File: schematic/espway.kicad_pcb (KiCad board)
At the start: 2 copper layers, 37.1 x 41.5 mm, 34 parts, among them J1 CONN_01X02, J2 CONN_01X02, J3 CONN_01X04_MALE, SW1 SW_Push, U1 DRV8835, U2 LM1117-3.3, U3 ESP-12E, U4 LSM6DS3

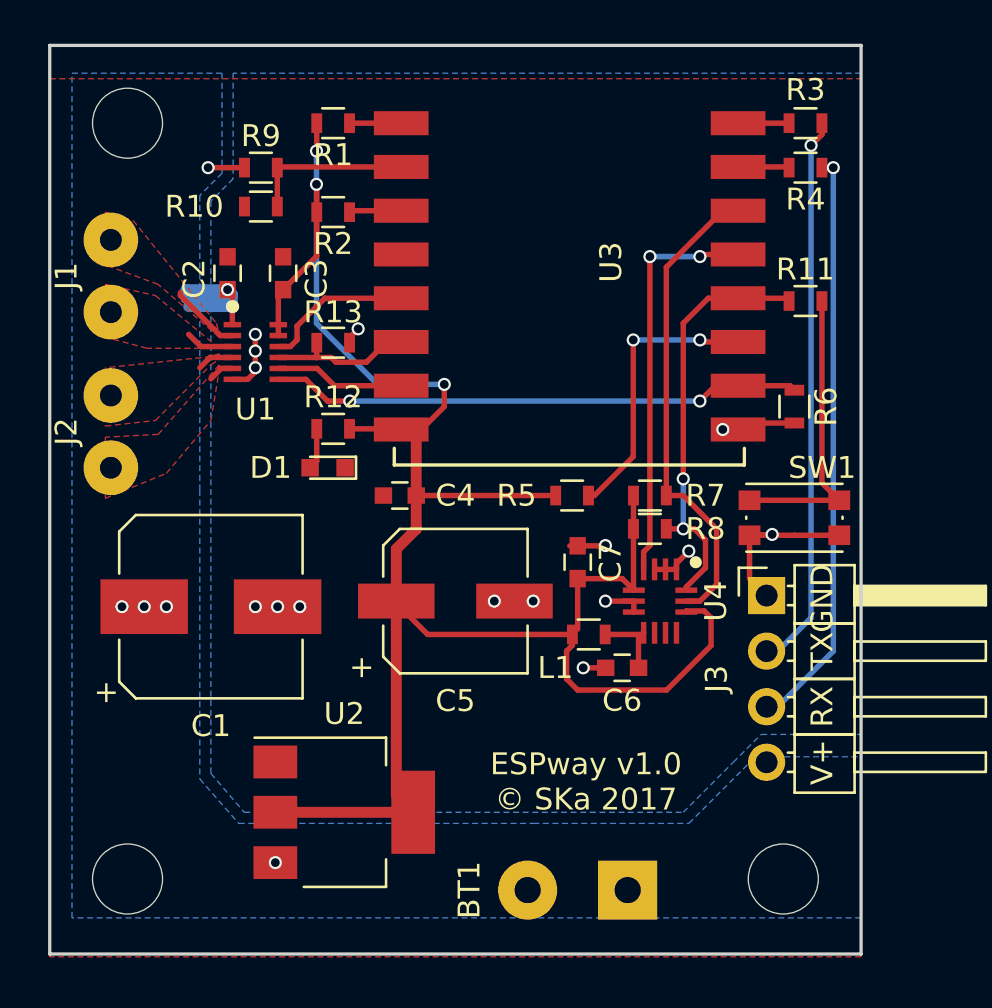
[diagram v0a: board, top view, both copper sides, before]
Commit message: PCB: improvements
Routing simplified
Use LGA-14 and WSON-12 packages supplied with KiCAD
diff --git a/schematic-old/espway-rescue.lib b/schematic-old/espway-rescue.lib
new file mode 100644
index 0000000..4d5fc14
--- /dev/null
+++ b/schematic-old/espway-rescue.lib
@@ -0,0 +1,25 @@
+EESchema-LIBRARY Version 2.3
+#encoding utf-8
+#
+# LM1117-5.0-RESCUE-espway
+#
+DEF LM1117-5.0-RESCUE-espway U 0 30 Y Y 1 F N
+F0 "U" 100 -250 50 H V C CNN
+F1 "LM1117-5.0-RESCUE-espway" 0 250 50 H V C CNN
+F2 "" 0 0 50 H V C CNN
+F3 "" 0 0 50 H V C CNN
+$FPLIST
+ SOT-223*
+ TO-263*
+ TO-252*
+$ENDFPLIST
+DRAW
+S -200 -200 200 200 0 1 10 f
+X GND/ADJ 1 0 -300 100 U 50 50 1 1 W
+X VO 2 300 0 100 L 50 50 1 1 w
+X VI 3 -300 0 100 R 50 50 1 1 W
+X VO 4 300 0 100 L 50 50 1 1 w N
+ENDDRAW
+ENDDEF
+#
+#End Library
diff --git a/schematic-old/espway.pro b/schematic-old/espway.pro
index d39d63e..2c69b71 100644
--- a/schematic-old/espway.pro
+++ b/schematic-old/espway.pro
@@ -1,4 +1,4 @@
-update=su  5. helmikuuta 2017 09.41.29
+update=2017 October 17, Tuesday 01:25:24
 version=1
 last_client=kicad
 [pcbnew]
@@ -25,43 +25,6 @@ version=1
 NetIExt=net
 [general]
 version=1
-[eeschema]
-version=1
-LibDir=
-[eeschema/libraries]
-LibName1=power
-LibName2=device
-LibName3=transistors
-LibName4=conn
-LibName5=linear
-LibName6=regul
-LibName7=74xx
-LibName8=cmos4000
-LibName9=adc-dac
-LibName10=memory
-LibName11=xilinx
-LibName12=microcontrollers
-LibName13=dsp
-LibName14=microchip
-LibName15=analog_switches
-LibName16=motorola
-LibName17=texas
-LibName18=intel
-LibName19=audio
-LibName20=interface
-LibName21=digital-audio
-LibName22=philips
-LibName23=display
-LibName24=cypress
-LibName25=siliconi
-LibName26=opto
-LibName27=atmel
-LibName28=contrib
-LibName29=valves
-LibName30=d1_mini
-LibName31=gy-521
-LibName32=ws2812b
-LibName33=l293d
 [schematic_editor]
 version=1
 PageLayoutDescrFile=
@@ -72,3 +35,41 @@ NetFmtName=
 SpiceForceRefPrefix=0
 SpiceUseNetNumbers=0
 LabSize=60
+[eeschema]
+version=1
+LibDir=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
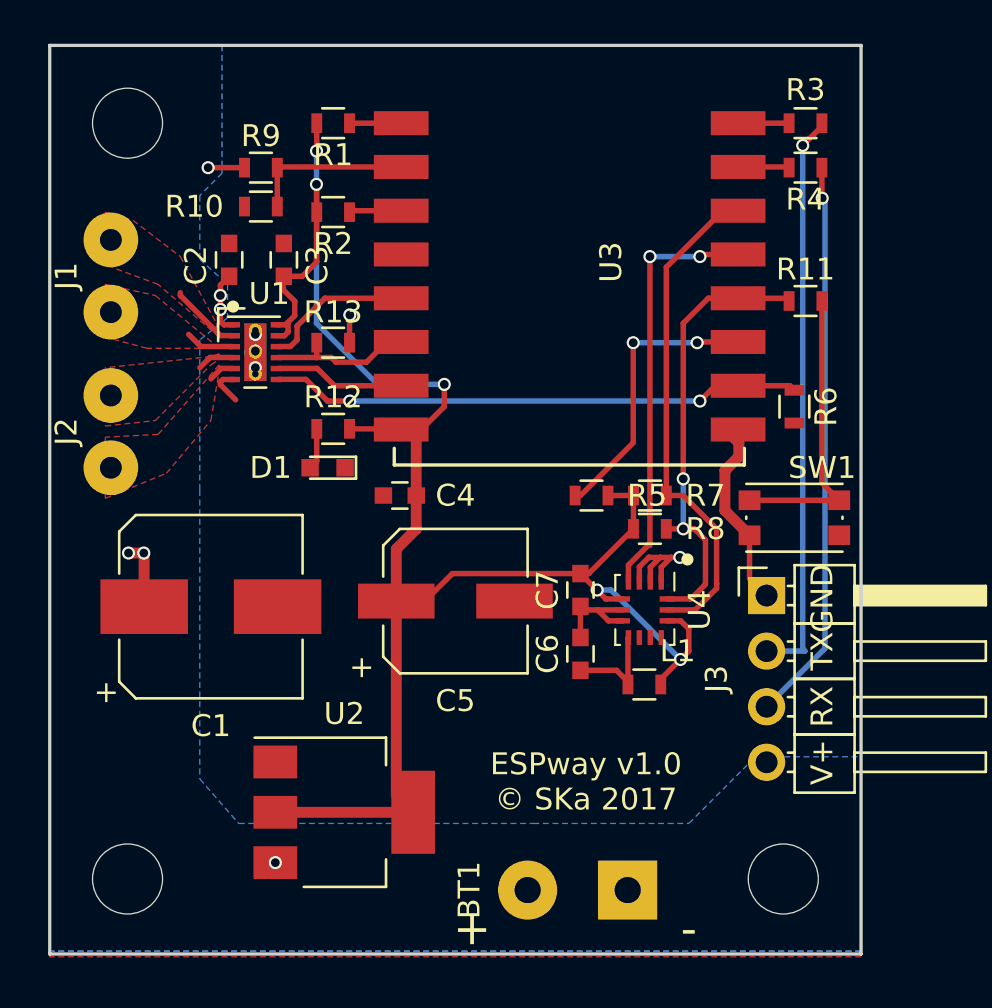
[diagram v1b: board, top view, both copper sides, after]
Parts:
- U1: footprint espway-modules:WSON-12 -> Housings_SON:WSON-12-1EP_3x2mm_Pitch0.5mm_ThermalVias
- U4: footprint espway-modules:LGA-14L -> Housings_LGA:Bosch_LGA-14_3x2.5mm_Pitch0.5mm
- moved L1 3.42 mm to (170.4, 108.0), turned to 0 degrees
- moved U1 2.74 mm to (152.7, 92.8)
- moved U4 2.09 mm to (170.5, 104.5)
- moved C6 2.01 mm to (167.5, 106.6), turned to 90 degrees
- moved C7 1.28 mm to (167.5, 103.6), turned to 90 degrees
- moved R5 0.89 mm to (168.0, 99.3), turned to 180 degrees
- moved C2 0.62 mm to (151.5, 88.5)
- moved C3 0.61 mm to (154.0, 88.5)
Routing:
- net +3V3: track 92.1 -> 83.7 mm, vias 3 -> 5
- net +BATT: track 12.7 -> 7.97 mm, vias 7 -> 6
- net GND: track 27.7 -> 24.7 mm, vias 15 -> 5
- net SDA: track 19.4 -> 20.8 mm
- net Net-(J3-Pad2): track 25.7 -> 27.1 mm
- net Net-(C6-Pad1): track 3.48 -> 4.72 mm
- net SCL: track 21.3 -> 22.5 mm
- net INT: track 17.8 -> 18.8 mm
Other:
- board text added: "+"
- board text added: "-"

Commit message: PCB update before rerouting
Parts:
- moved R6 25.5 mm to (151.9, 96.9)
- moved R11 21.4 mm to (173.2, 111.4), turned to 270 degrees
- moved SW1 13.7 mm to (169.1, 111.3)
- moved R5 9.80 mm to (172.6, 108.0), turned to 0 degrees
- moved C4 3.52 mm to (156.7, 96.9), turned to 270 degrees
- moved D1 2.73 mm to (153.5, 96.9), turned to 90 degrees
- moved R4 1.52 mm to (177.3, 85.7), turned to 90 degrees
- moved C2 1.46 mm to (152.8, 89.2)
- moved R12 1.34 mm to (155.1, 96.9), turned to 90 degrees
- moved BT1 1.02 mm to (165.1, 116.3)
- moved R3 1.01 mm to (177.3, 83.1), turned to 90 degrees
- moved J2 0.90 mm to (146.9, 104.8)
- moved J1 0.89 mm to (146.9, 90.9)
- moved C3 0.78 mm to (154.4, 89.2)
- moved L1 0.66 mm to (169.8, 108.0)
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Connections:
- R3 pad 1: Net-(J3-Pad2) -> Net-(J3-Pad3)
- R4 pad 1: Net-(J3-Pad3) -> Net-(J3-Pad2)
- U3 pad 11: Net-(R5-Pad2) -> SCL
- U3 pad 14: SCL -> Net-(U3-Pad14)
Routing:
- net GND: track 24.7 -> 43.8 mm, vias 5 -> 18
- net Net-(U3-Pad14): track 0.00 -> 16.7 mm
- net SCL: track 22.5 -> 37.4 mm
- net INT: track 18.8 -> 6.15 mm, vias 2 -> 0
- net Net-(R5-Pad2): track 12.5 -> 2.16 mm, vias 2 -> 0
- net Net-(R11-Pad2): track 13.7 -> 6.95 mm
- net Net-(J3-Pad2): track 27.1 -> 20.6 mm, vias 1 -> 0
- net ADC: track 8.15 -> 13.1 mm
- net Net-(J2-Pad1): track 1.18 -> 4.55 mm
- net Net-(R2-Pad1): track 3.09 -> 0.09 mm
- net +BATT: track 7.97 -> 5.53 mm, vias 6 -> 0
- net Net-(J1-Pad1): track 2.23 -> 4.17 mm
- net Net-(J2-Pad2): track 1.68 -> 3.58 mm
- net Net-(J1-Pad2): track 3.27 -> 4.21 mm
- net GPIO15: track 24.5 -> 25.2 mm
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- added copper zone on F.Cu, net +BATT
- removed copper zone on B.Cu, net +BATT
- removed copper zone on F.Cu, net GND
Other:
- board size 37.1 x 41.5 mm -> 37.1 x 41.7 mm
- board text removed: "ESPway v1.0 © SKa 2017"

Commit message: Initial work on new PCB
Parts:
- removed ?: MountingHole_2.2mm_M2, Mounting_Holes:MountingHole_3.2mm_M3
- removed the REF** at (176.8, 116.8)
- removed the REF** at (146.8, 82.3)
- added R14: 2k2, Resistors_SMD:R_0603, F.Cu at (135.2, 134.5)
- added REF**: MountingHole_3.2mm_M3, Mounting_Holes:MountingHole_3.2mm_M3, F.Cu at (129.5, 154.0)
- added REF**: MountingHole_3.2mm_M3, Mounting_Holes:MountingHole_3.2mm_M3, F.Cu at (162.5, 123.8)
- added REF**: MountingHole_3.2mm_M3, Mounting_Holes:MountingHole_3.2mm_M3, F.Cu at (129.5, 124.0)
- C1: value 470u -> 100n; footprint Capacitors_SMD:CP_Elec_8x10 -> Capacitors_SMD:C_0603
- C2: value 100n -> 470u; footprint Capacitors_SMD:C_0603 -> Capacitors_SMD:CP_Elec_8x10
- C4: value 100n -> 100u; footprint Capacitors_SMD:C_0603 -> Capacitors_SMD:CP_Elec_6.3x5.8
- C5: value 100u -> 100n; footprint Capacitors_SMD:CP_Elec_6.3x5.8 -> Capacitors_SMD:C_0603
- R10, R5, R6: value 10k -> 470
- R11: value 470 -> 82k
- R12, R4: value 470 -> 10k
- R13: value 10k -> 2k2
- R7, R8: value 2k2 -> 10k
- R9: value 82k -> 10k
- U1: value DRV8835 -> LM1117-3.3; footprint Housings_SON:WSON-12-1EP_3x2mm_Pitch0.5mm_ThermalVias -> TO_SOT_Packages_SMD:SOT-223
- U2: value LM1117-3.3 -> ESP-12E; footprint TO_SOT_Packages_SMD:SOT-223 -> ESP8266:ESP-12E_SMD
- U3: value ESP-12E -> DRV8835; footprint ESP8266:ESP-12E_SMD -> espway-modules:WSON-12
- U4: footprint Housings_LGA:Bosch_LGA-14_3x2.5mm_Pitch0.5mm -> espway-modules:LGA-14L
- moved R3 69.3 mm to (135.5, 138.5), turned to 270 degrees
- moved R1 56.5 mm to (129.2, 132.0), turned to 270 degrees
- moved R10 55.7 mm to (149.8, 141.8), turned to 90 degrees
- moved C4 54.6 mm to (132.2, 145.8)
- moved U1 54.5 mm to (139.8, 145.8), turned to 90 degrees
- moved C2 54.0 mm to (162.5, 142.2), turned to 180 degrees
- moved U4 50.7 mm to (129.5, 134.5)
- moved L1 50.7 mm to (130.0, 139.5), turned to 180 degrees
- moved C7 49.3 mm to (129.2, 134.8)
- moved C6 48.8 mm to (130.0, 137.8), turned to 180 degrees
- moved R9 48.0 mm to (158.5, 132.0)
- moved J3 47.7 mm to (154.5, 146.5), turned to 270 degrees
- moved C3 47.6 mm to (164.0, 135.8), turned to 90 degrees
- moved U3 47.3 mm to (163.0, 129.5), turned to 180 degrees
- moved R2 47.2 mm to (133.5, 127.8), turned to 270 degrees
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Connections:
- C1 pad 1: +BATT -> +3V3
- C2 pad 1: GND -> +BATT
- C2 pad 2: +BATT -> GND
- C3 pad 2: +3V3 -> +BATT
- C5 pad 1: +3V3 -> GND
- C5 pad 2: GND -> +3V3
- R10 pad 1: ADC -> Net-(R10-Pad1)
- R11 pad 1: SDA -> +BATT
- R11 pad 2: Net-(R11-Pad2) -> ADC
- R12 pad 1: Net-(D1-Pad2) -> ADC
- R12 pad 2: +3V3 -> GND
- R13 pad 1: Net-(R13-Pad1) -> +3V3
- R13 pad 2: GND -> SCL
- R3 pad 1: Net-(J3-Pad3) -> Net-(D1-Pad2)
- R3 pad 2: Net-(R3-Pad2) -> +3V3
- R4 pad 1: Net-(J3-Pad2) -> BENBL
- R4 pad 2: Net-(R4-Pad2) -> GND
- R5 pad 1: +3V3 -> Net-(J3-Pad3)
- R6 pad 1: GPIO15 -> Net-(J3-Pad2)
- R6 pad 2: GND -> Net-(R6-Pad2)
- R7 pad 1: +3V3 -> AENBL
- R7 pad 2: SCL -> GND
- R8 pad 1: +3V3 -> APHASE
- R8 pad 2: SDA -> GND
- R9 pad 1: +BATT -> +3V3
- R9 pad 2: ADC -> BPHASE
- SW1 pad 1: GND -> Net-(R10-Pad1)
- SW1 pad 2: Net-(R11-Pad2) -> BPHASE
- U1 pad 1: +BATT -> GND
- U1 pad 2: Net-(J1-Pad2) -> +3V3
- U1 pad 3: Net-(J1-Pad1) -> +BATT
- U1 pad 4: Net-(J2-Pad2) -> +3V3
- U2 pad 1: GND -> Net-(R1-Pad1)
- U2 pad 2: +3V3 -> ADC
- U2 pad 3: +BATT -> Net-(R2-Pad1)
- U2 pad 4: +3V3 -> Net-(U2-Pad4)
- U3 pad 1: Net-(R1-Pad1) -> +BATT
- U3 pad 10: GPIO15 -> APHASE
- U3 pad 11: SCL -> +3V3
- U3 pad 12: SDA -> +3V3
- U3 pad 13: INT -> GND
- U3 pad 2: ADC -> Net-(J1-Pad2)
- U3 pad 3: Net-(R2-Pad1) -> Net-(J1-Pad1)
- U3 pad 4: Net-(U3-Pad4) -> Net-(J2-Pad2)
- U3 pad 5: Net-(U1-Pad10) -> Net-(J2-Pad1)
- U3 pad 6: Net-(R13-Pad1) -> GND
- U3 pad 7: Net-(U1-Pad8) -> BENBL
- U3 pad 8: +3V3 -> BPHASE
- U3 pad 9: GND -> AENBL
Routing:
- net +BATT: track 5.53 -> 57.6 mm
- net GND: track 43.8 -> 7.07 mm, vias 18 -> 0
- net SCL: track 37.4 -> 7.84 mm
- net GPIO15: track 25.2 -> 0.00 mm, vias 2 -> 0
- net +3V3: track 83.9 -> 60.6 mm
- net Net-(J3-Pad3): track 26.5 -> 5.31 mm
- net BPHASE: track 0.00 -> 19.2 mm
- net Net-(U3-Pad14): track 16.7 -> 0.00 mm
- net Net-(J3-Pad2): track 20.6 -> 5.64 mm
- net SDA: track 21.2 -> 7.45 mm
- net Net-(R1-Pad1): track 3.06 -> 15.5 mm
- net (no net): track 0.00 -> 11.5 mm
- net APHASE: track 0.00 -> 10.2 mm
- net AENBL: track 0.00 -> 10.1 mm
- net Net-(R13-Pad1): track 9.15 -> 0.00 mm
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- removed copper zone on F.Cu, net +BATT
- removed copper zone on B.Cu, net GND
- removed copper zone on F.Cu, net Net-(J1-Pad1)
- removed copper zone on F.Cu, net Net-(J1-Pad2)
- removed copper zone on F.Cu, net Net-(J2-Pad1)
- removed copper zone on F.Cu, net Net-(J2-Pad2)
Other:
- board outline removed
- net class Default: clearance 0.16 -> 0.2
- rule pad_to_mask_clearance: 0.2 -> 0
- rule trace_clearance: 0.16 -> 0.2
- board text removed: "+"
- board text removed: "-"
- board text removed: "GND"
- board text removed: "RX"
- board text removed: "TX"
- board text removed: "V+"

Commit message: Committing before rerouting
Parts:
- added REF**: MountingHole_3.2mm_M3, Mounting_Holes:MountingHole_3.2mm_M3, F.Cu at (162.0, 154.0)
- moved BT1 4.15 mm to (167.8, 148.6), turned to 270 degrees
- moved R2 3.50 mm to (137.0, 127.7)
- moved R11 3.40 mm to (133.6, 127.8)
- moved R9 1.00 mm to (158.5, 131.0)
- moved REF** 0.56 mm to (162.0, 124.0)
- moved J1 0.32 mm to (167.8, 126.5)
- moved R10 0.25 mm to (150.0, 141.8)
- moved R5 0.25 mm to (146.0, 141.8)
- moved R6 0.25 mm to (147.8, 141.8)
- moved J2 0.20 mm to (167.8, 120.0)
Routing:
- net +3V3: track 60.6 -> 94.6 mm
- net Net-(R5-Pad2): track 0.00 -> 21.7 mm
- net Net-(R6-Pad2): track 0.00 -> 18.9 mm
- net GND: track 7.07 -> 21.4 mm, vias 0 -> 10
- net +BATT: track 57.6 -> 69.7 mm
- net (no net): track 11.5 -> 0.00 mm
- net BPHASE: track 19.2 -> 28.3 mm
- net Net-(R2-Pad1): track 7.90 -> 3.21 mm
- net ADC: track 6.06 -> 9.16 mm
- net Net-(J1-Pad2): track 2.01 -> 0.00 mm
- net Net-(J2-Pad2): track 1.91 -> 0.00 mm
- net Net-(J1-Pad1): track 1.91 -> 0.00 mm
- net Net-(J2-Pad1): track 1.41 -> 0.00 mm
- added copper zone on B.Cu, net GND
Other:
- board outline added: 44.5 x 37 mm

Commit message: An intermediate commit
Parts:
- moved J3 25.7 mm to (130.2, 138.0), turned to 180 degrees
- moved L1 24.8 mm to (153.0, 148.8), turned to 270 degrees
- moved C7 24.3 mm to (148.5, 149.5), turned to 180 degrees
- moved C6 24.2 mm to (151.5, 148.8), turned to 270 degrees
- moved U4 23.8 mm to (148.3, 149.1), turned to 0 degrees
- moved R6 15.3 mm to (133.8, 135.5), turned to 0 degrees
- moved R5 14.5 mm to (133.8, 134.0), turned to 0 degrees
- moved R14 13.8 mm to (147.0, 141.8)
- moved R13 13.6 mm to (148.5, 141.8)
- moved R1 4.51 mm to (133.5, 130.5)
- moved C4 2.21 mm to (134.2, 144.8)
- moved U1 1.79 mm to (141.3, 144.8)
- moved R2 0.10 mm to (137.0, 127.8)
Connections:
- U2 pad 5: INT -> SCL
- U2 pad 7: SCL -> INT
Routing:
- net +3V3: track 94.6 -> 0.00 mm
- net +BATT: track 69.7 -> 0.00 mm
- net BPHASE: track 28.3 -> 0.00 mm
- net Net-(R5-Pad2): track 21.7 -> 0.00 mm
- net GND: track 21.4 -> 0.00 mm, vias 10 -> 0
- net Net-(R6-Pad2): track 18.9 -> 0.00 mm
- net Net-(R1-Pad1): track 15.5 -> 0.00 mm
- net INT: track 10.5 -> 0.00 mm
- net APHASE: track 10.2 -> 0.00 mm
- net AENBL: track 10.1 -> 0.00 mm
- net ADC: track 9.16 -> 0.00 mm
- net BENBL: track 8.31 -> 0.00 mm
- net SCL: track 7.85 -> 0.00 mm
- net SDA: track 7.45 -> 0.00 mm
- net Net-(R10-Pad1): track 6.07 -> 0.00 mm
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
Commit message: PCB: stable checkpoint
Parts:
- moved BT1 25.5 mm to (142.5, 151.5), turned to 180 degrees
- moved R1 6.95 mm to (137.0, 124.5)
- moved R5 3.91 mm to (135.5, 130.5)
- moved R6 3.69 mm to (135.5, 132.2)
- moved D1 3.64 mm to (135.0, 135.0), turned to 270 degrees
- moved R10 3.55 mm to (152.2, 144.5), turned to 0 degrees
- moved R11 3.54 mm to (135.0, 124.5)
- moved REF** 3.16 mm to (130.5, 151.0)
- moved REF** 3.00 mm to (162.0, 151.0)
- moved R7 2.06 mm to (158.0, 133.8)
- moved R8 2.02 mm to (160.0, 133.8)
- moved C4 1.63 mm to (133.0, 143.8), turned to 180 degrees
- moved R14 1.60 mm to (148.2, 142.8), turned to 180 degrees
- moved R4 1.58 mm to (158.0, 130.5), turned to 270 degrees
- moved R9 1.58 mm to (160.0, 130.5), turned to 270 degrees
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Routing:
- net +3V3: track 0.00 -> 115.1 mm
- net +BATT: track 0.00 -> 51.7 mm
- net GND: track 0.00 -> 45.2 mm, vias 0 -> 16
- net BPHASE: track 0.00 -> 23.2 mm
- net Net-(R5-Pad2): track 0.00 -> 21.8 mm
- net Net-(R6-Pad2): track 0.00 -> 21.7 mm
- net SCL: track 0.00 -> 17.6 mm
- net INT: track 0.00 -> 15.3 mm
- net SDA: track 0.00 -> 15.2 mm
- net ADC: track 0.00 -> 8.98 mm
- net APHASE: track 0.00 -> 8.50 mm
- net BENBL: track 0.00 -> 8.31 mm
- net AENBL: track 0.00 -> 7.90 mm
- net Net-(J2-Pad1): track 0.00 -> 6.18 mm
- net Net-(R10-Pad1): track 0.00 -> 6.13 mm
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- added copper zone on F.Cu, net +BATT
- added copper zone on F.Cu, net Net-(J1-Pad1)
- added copper zone on F.Cu, net Net-(J1-Pad2)
- added copper zone on F.Cu, net Net-(J2-Pad1)
- added copper zone on F.Cu, net Net-(J2-Pad2)
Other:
- board size 44.5 x 37 mm -> 43 x 33.2 mm
- board text added: "+"
- board text added: "-"
- board text added: "ESPway rev 2 SKa, 2017"
- board text added: "GND"
- board text added: "RX"
- board text added: "TX"
- board text added: "V+"
